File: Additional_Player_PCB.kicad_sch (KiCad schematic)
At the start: 10 parts, among them J1 Conn_01x10, SW1 CherryMX, SW2 CherryMX, SW3 CherryMX, SW4 CherryMX, SW5 CherryMX, SW6 CherryMX, SW7 CherryMX, SW8 CherryMX, SW9 CherryMX

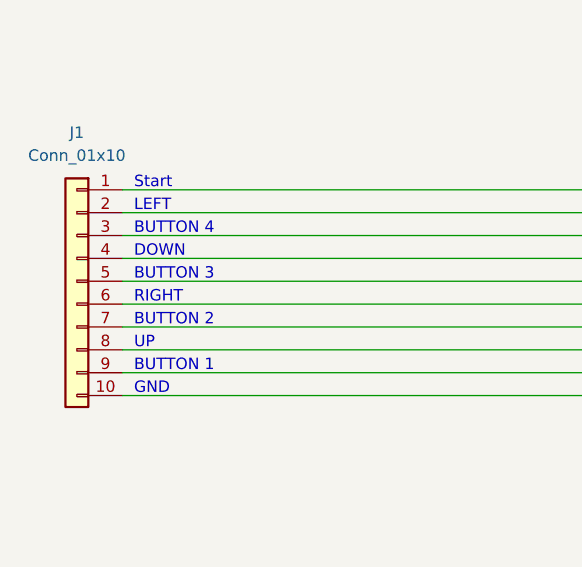
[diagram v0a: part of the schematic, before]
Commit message: Net Names Added
Didn't realize that annotations didn't function as official net names. Fixed now.
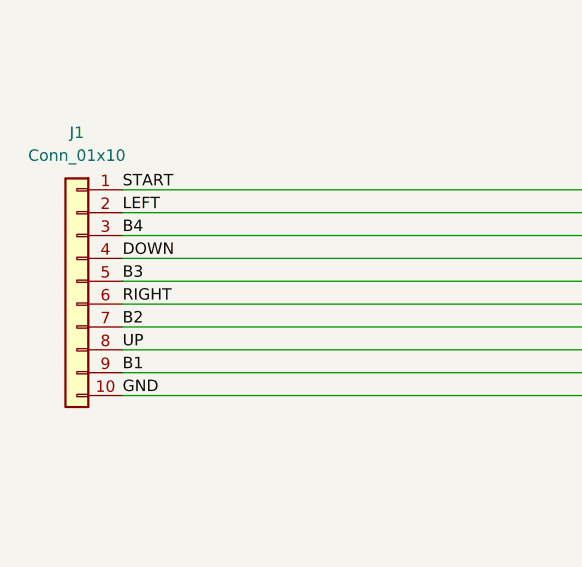
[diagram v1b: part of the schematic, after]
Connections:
- net LEFT: now reaches J1.2 (Pin_2), SW3.1
- net GND: now reaches J1.10 (Pin_10), SW1.2, SW2.2, SW3.2, SW4.2, SW5.2, SW6.2, SW7.2, SW8.2, SW9.2
- net B4: now reaches J1.3 (Pin_3), SW9.1
- net B1: now reaches J1.9 (Pin_9), SW6.1
- net B3: now reaches J1.5 (Pin_5), SW8.1
- net START: now reaches J1.1 (Pin_1), SW1.1
- net DOWN: now reaches J1.4 (Pin_4), SW4.1
- net RIGHT: now reaches J1.6 (Pin_6), SW5.1
- net B2: now reaches J1.7 (Pin_7), SW7.1
- net UP: now reaches J1.8 (Pin_8), SW2.1
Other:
- note removed: "BUTTON 1"
- note removed: "BUTTON 2"
- note removed: "BUTTON 3"
- note removed: "BUTTON 4"
- note removed: "DOWN"
- note removed: "GND"
- note removed: "LEFT"
- note removed: "RIGHT"
- note removed: "Start"
- note removed: "UP"
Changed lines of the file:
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@@
     (stroke (width 0) (type default) (color 0 0 0 0))
   )
-  (text "BUTTON 3\n" (at 40.64 92.71 0)
+  (label "B4" (at 39.37 87.63 0)
     (effects (font (size 1.27 1.27)) (justify left bottom))
   )
-  (text "DOWN\n" (at 40.64 90.17 0)
+  (label "UP" (at 39.37 100.33 0)
     (effects (font (size 1.27 1.27)) (justify left bottom))
   )
-  (text "Start\n" (at 40.64 82.55 0)
+  (label "START" (at 39.37 82.55 0)
     (effects (font (size 1.27 1.27)) (justify left bottom))
   )
-  (text "BUTTON 1" (at 40.64 102.87 0)
+  (label "GND" (at 39.37 105.41 0)
     (effects (font (size 1.27 1.27)) (justify left bottom))
   )
-  (text "UP" (at 40.64 100.33 0)
+  (label "B2" (at 39.37 97.79 0)
     (effects (font (size 1.27 1.27)) (justify left bottom))
   )
-  (text "BUTTON 2" (at 40.64 97.79 0)
+  (label "RIGHT" (at 39.37 95.25 0)
     (effects (font (size 1.27 1.27)) (justify left bottom))
   )
-  (text "GND" (at 40.64 105.41 0)
+  (label "B1" (at 39.37 102.87 0)
     (effects (font (size 1.27 1.27)) (justify left bottom))
   )
-  (text "RIGHT\n" (at 40.64 95.25 0)
+  (label "B3" (at 39.37 92.71 0)
     (effects (font (size 1.27 1.27)) (justify left bottom))
   )
-  (text "BUTTON 4" (at 40.64 87.63 0)
+  (label "LEFT" (at 39.37 85.09 0)
     (effects (font (size 1.27 1.27)) (justify left bottom))
   )
-  (text "LEFT\n" (at 40.64 85.09 0)
+  (label "DOWN" (at 39.37 90.17 0)
     (effects (font (size 1.27 1.27)) (justify left bottom))
   )

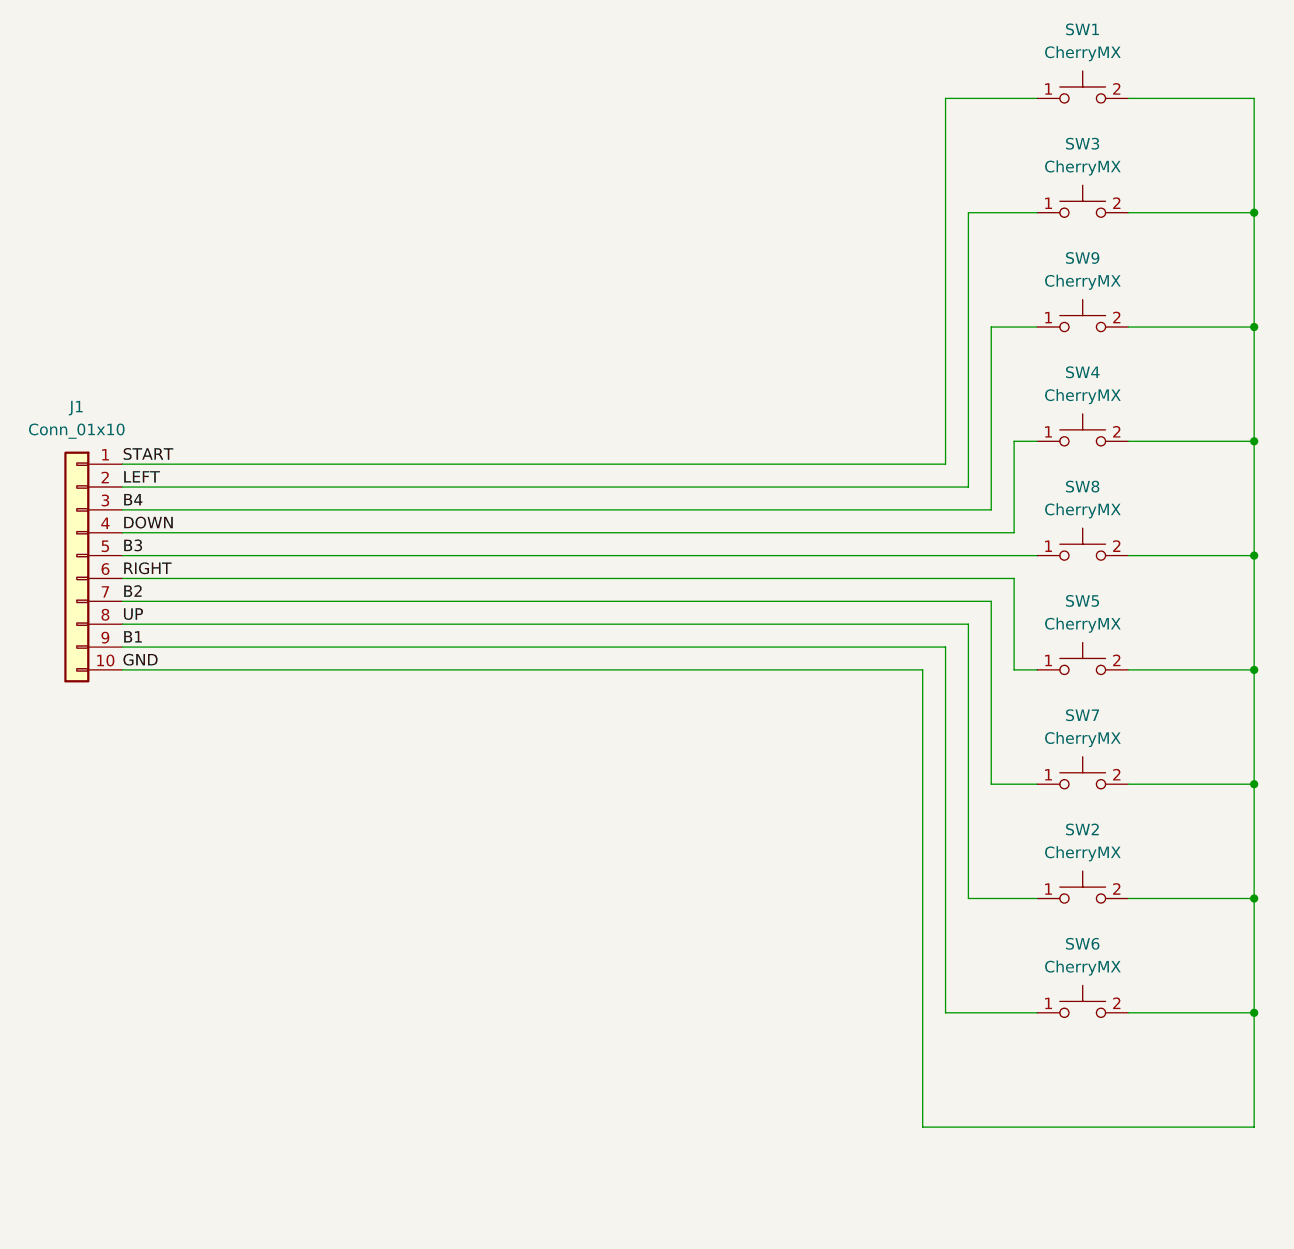
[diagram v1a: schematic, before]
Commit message: Correct J1 connector
Mil vs. MM, what's the deal?
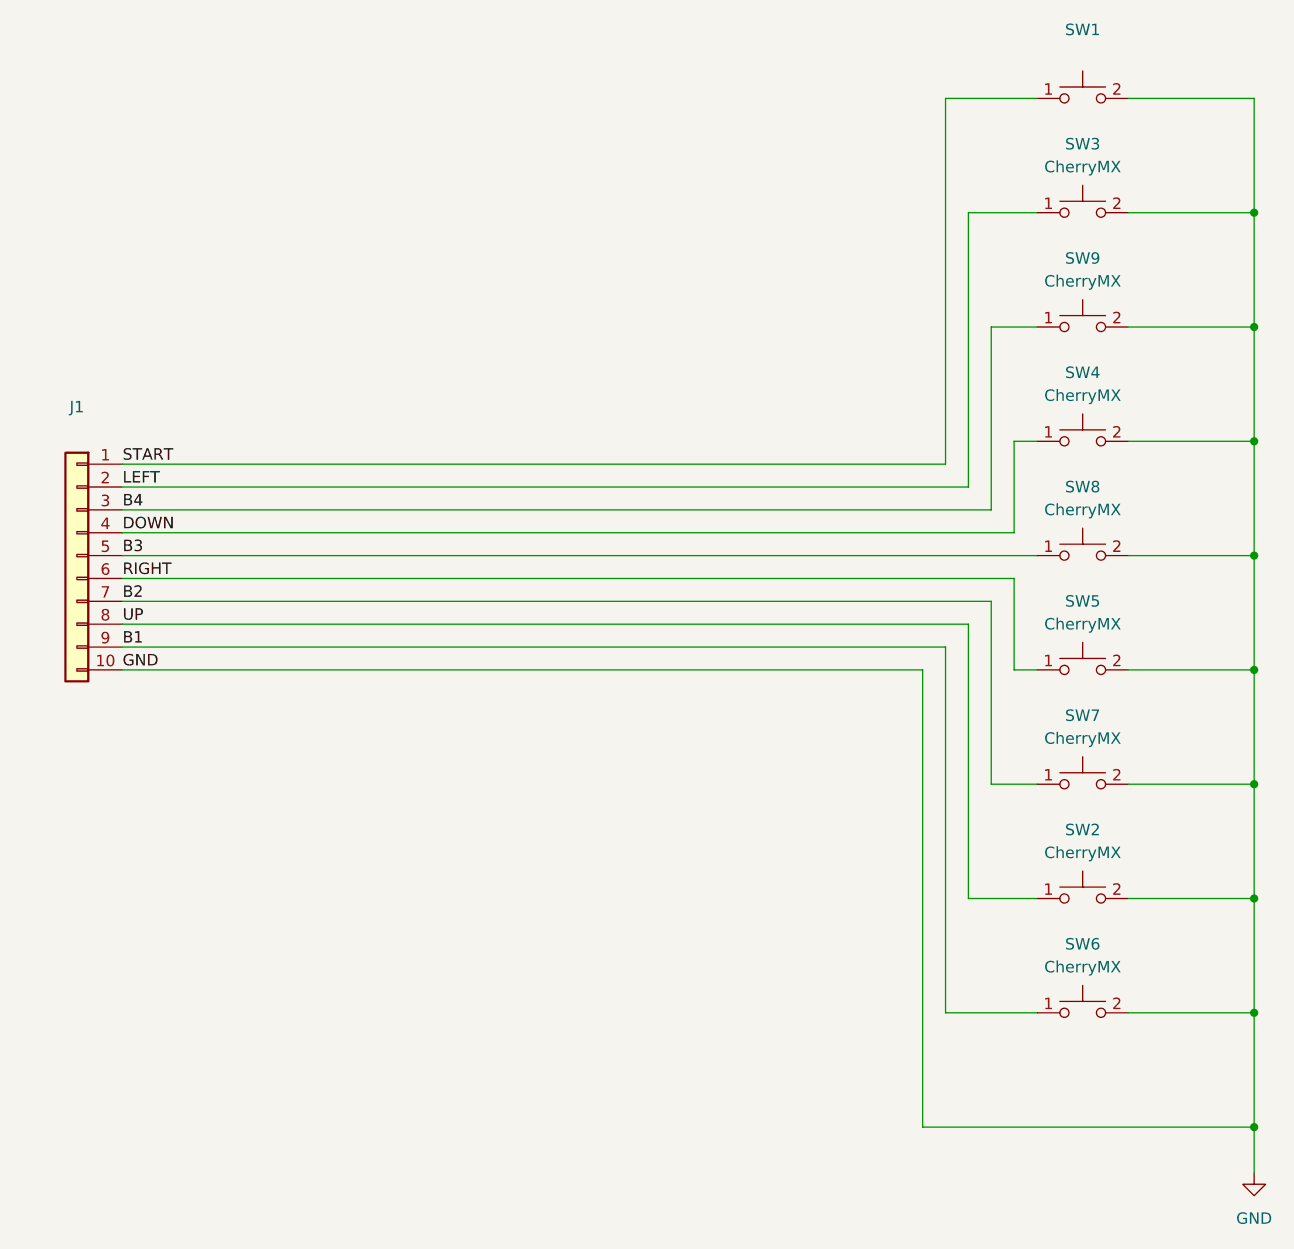
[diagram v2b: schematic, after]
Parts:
- J1: value Conn_01x10 -> (none); footprint Connector_PinHeader_1.00mm:PinHeader_2x05_P1.00mm_Vertical -> (none)
- SW1: value CherryMX -> (none); footprint Button_Switch_Keyboard:SW_Cherry_MX_1.00u_PCB -> (none)
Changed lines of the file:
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@@
     (comment 1 "This is one dope schematic.")
   )
+  (junction (at 165.1 156.21) (diameter 0) (color 0 0 0 0)
+  )
   (junction (at 165.1 130.81) (diameter 0) (color 0 0 0 0)
   )
@@
   )
   (wire (pts (xy 135.89 67.31) (xy 140.97 67.31))
+    (stroke (width 0) (type default) (color 0 0 0 0))
+  )
+  (wire (pts (xy 165.1 156.21) (xy 165.1 161.29))
     (stroke (width 0) (type default) (color 0 0 0 0))
   )
@@
     (pin "2")
   )
+  (symbol (lib_id "power:GND") (at 165.1 161.29 0) (unit 1)
+    (in_bom yes) (on_board yes) (fields_autoplaced)
+    (property "Reference" "#PWR01" (id 0) (at 165.1 167.64 0)
+      (effects (font (size 1.27 1.27)) hide)
+    )
+    (property "Value" "GND" (id 1) (at 165.1 166.37 0))
+    (property "Footprint" "" (id 2) (at 165.1 161.29 0)
+      (effects (font (size 1.27 1.27)) hide)
+    )
+    (property "Datasheet" "" (id 3) (at 165.1 161.29 0)
+      (effects (font (size 1.27 1.27)) hide)
+    )
+    (pin "1")
+  )
   (symbol (lib_id "Connector_Generic:Conn_01x10") (at 34.29 92.71 0) (mirror y) (unit 1)
     (in_bom yes) (on_board yes) (fields_autoplaced)
     (property "Reference" "J1" (id 0) (at 34.29 76.2 0))
-    (property "Value" "Conn_01x10" (id 1) (at 34.29 78.74 0))
-    (property "Footprint" "Connector_PinHeader_1.00mm:PinHeader_2x05_P1.00mm_Vertical" (id 2) (at 34.29 92.71 0)
+    (property "Value" "" (id 1) (at 34.29 78.74 0))
+    (property "Footprint" "" (id 2) (at 34.29 92.71 0)
       (effects (font (size 1.27 1.27)) hide)
     )
@@
     (in_bom yes) (on_board yes)
     (property "Reference" "SW1" (id 0) (at 146.05 34.29 0))
-    (property "Value" "CherryMX" (id 1) (at 146.05 36.83 0))
-    (property "Footprint" "Button_Switch_Keyboard:SW_Cherry_MX_1.00u_PCB" (id 2) (at 146.05 41.275 0)
+    (property "Value" "" (id 1) (at 146.05 36.83 0))
+    (property "Footprint" "" (id 2) (at 146.05 41.275 0)
       (effects (font (size 1.27 1.27)) hide)
     )
@@
   )
   (symbol_instances
+    (path "/5a319d05-1a85-43fe-a179-ebcee7212a03"
+      (reference "#PWR01") (unit 1) (value "GND") (footprint "")
+    )
     (path "/823cee59-0d64-4a43-b327-fc133b579150"
-      (reference "J1") (unit 1) (value "Conn_01x10") (footprint "Connector_PinHeader_1.00mm:PinHeader_2x05_P1.00mm_Vertical")
+      (reference "J1") (unit 1) (value "PinHeader_2x05_P2.54mm_Vertical") (footprint "Connector_PinHeader_2.54mm:PinHeader_2x05_P2.54mm_Vertical")
     )
     (path "/d99126ad-76d0-4e11-8b29-f88759ff2a24"
